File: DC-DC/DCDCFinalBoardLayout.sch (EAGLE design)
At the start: 38 parts, among them K1 ALZ12B12W, Q1 BUZ10, Q2 BUZ10

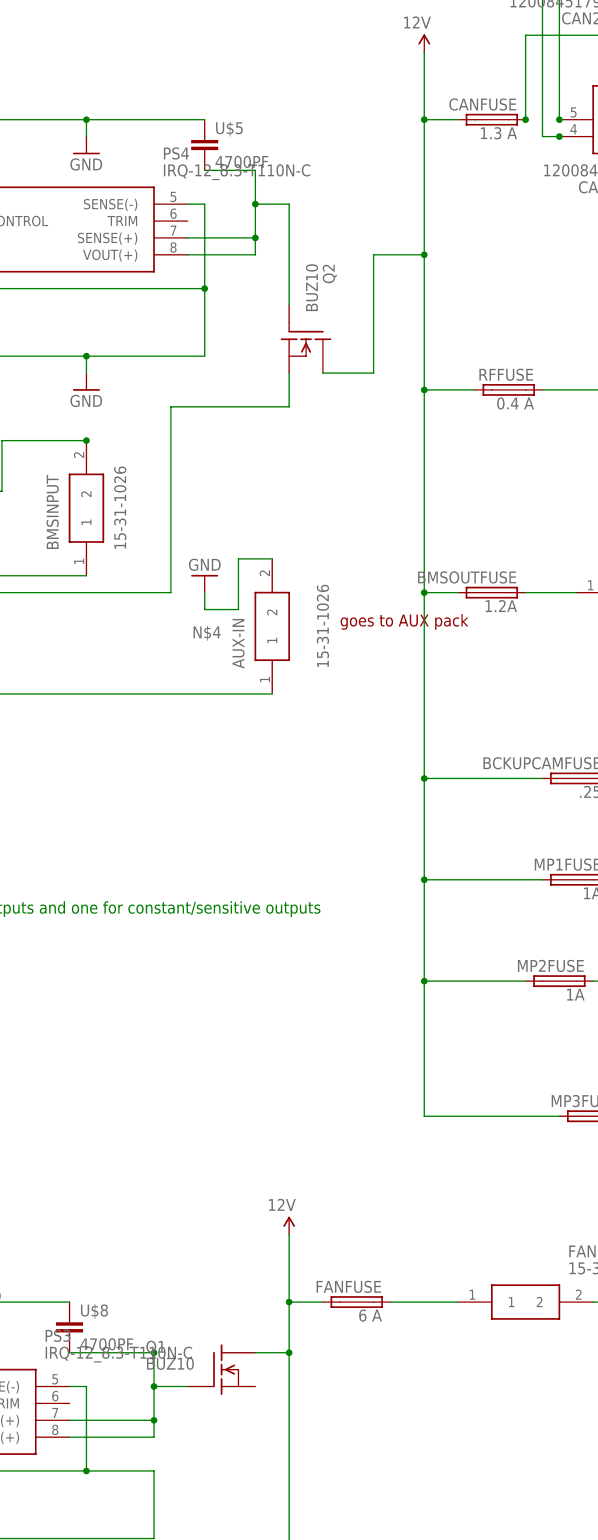
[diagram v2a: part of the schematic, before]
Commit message: updated DCDC diode
replaced insufficient SMD diode (in terms of current cap) with three TO220 diodes, with parallel dual configurations
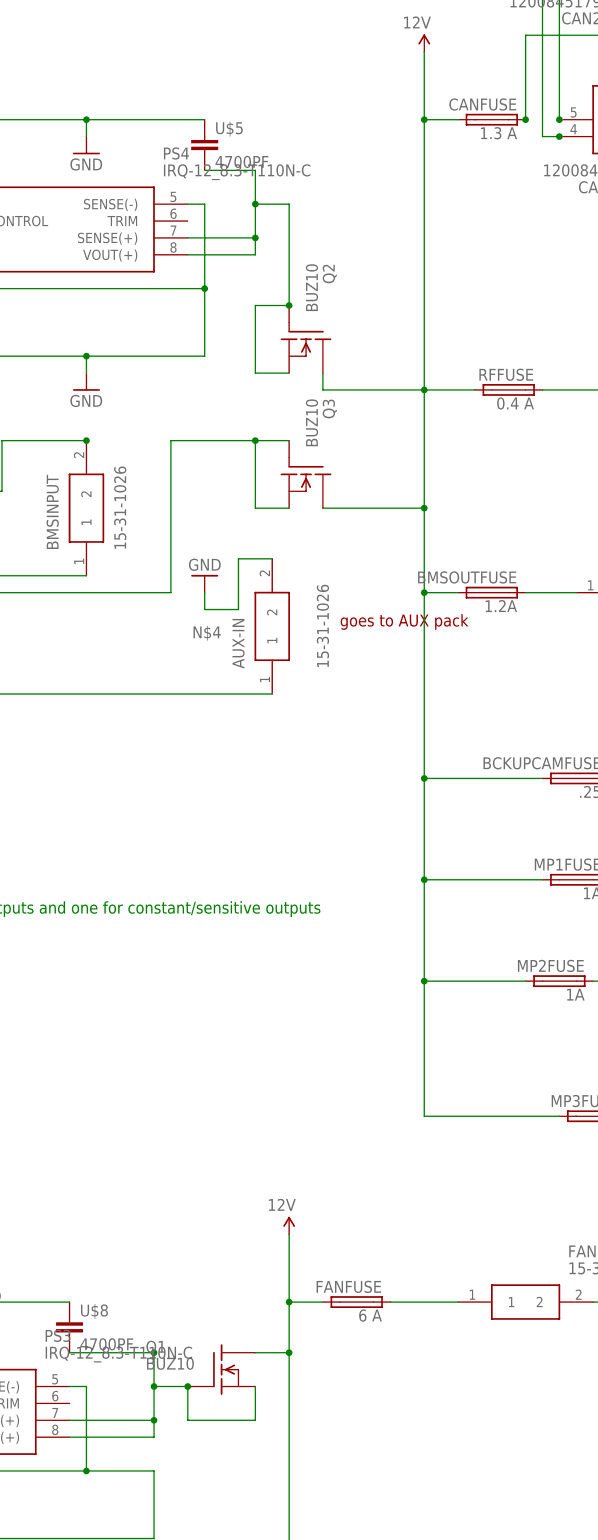
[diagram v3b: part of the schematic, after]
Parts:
- added Q3: BUZ10, transistor-fet:BUZ10
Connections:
- net 12V: now also Q3.D
- net N$13: now also Q1.S
- net N$15: now also Q2.S
- net N$4: now also Q3.G, Q3.S; no longer Q2.S
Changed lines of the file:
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@@
 <?xml version="1.0" encoding="utf-8"?>
 <!DOCTYPE eagle SYSTEM "eagle.dtd">
-<eagle version="9.5.1">
+<eagle version="9.1.1">
 <drawing>
 <settings>
@@
 <part name="Q2" library="transistor-fet" library_urn="urn:adsk.eagle:library:396" deviceset="BUZ10" device="" package3d_urn="urn:adsk.eagle:package:28520/1"/>
 <part name="Q1" library="transistor-fet" library_urn="urn:adsk.eagle:library:396" deviceset="BUZ10" device="" package3d_urn="urn:adsk.eagle:package:28520/1"/>
+<part name="Q3" library="transistor-fet" library_urn="urn:adsk.eagle:library:396" deviceset="BUZ10" device="" package3d_urn="urn:adsk.eagle:package:28520/1"/>
 </parts>
 <sheets>
@@
 <attribute name="VALUE" x="-204.47" y="-50.8" size="1.778" layer="96"/>
 <attribute name="NAME" x="-204.47" y="-48.26" size="1.778" layer="95"/>
+</instance>
+<instance part="Q3" gate="G$1" x="-180.34" y="83.82" smashed="yes" rot="R270">
+<attribute name="VALUE" x="-180.34" y="95.25" size="1.778" layer="96" rot="R270"/>
+<attribute name="NAME" x="-177.8" y="95.25" size="1.778" layer="95" rot="R270"/>
 </instance>
 </instances>
@@
 <wire x1="-162.56" y1="137.16" x2="-162.56" y2="147.32" width="0.1524" layer="91"/>
 <junction x="-162.56" y="137.16"/>
-<wire x1="-162.56" y1="137.16" x2="-162.56" y2="116.84" width="0.1524" layer="91"/>
-<wire x1="-162.56" y1="116.84" x2="-162.56" y2="96.52" width="0.1524" layer="91"/>
+<wire x1="-162.56" y1="137.16" x2="-162.56" y2="96.52" width="0.1524" layer="91"/>
 <pinref part="RFFUSE" gate="F1" pin="2"/>
 <wire x1="-162.56" y1="96.52" x2="-154.94" y2="96.52" width="0.1524" layer="91"/>
 <junction x="-162.56" y="96.52"/>
-<wire x1="-170.18" y1="116.84" x2="-162.56" y2="116.84" width="0.1524" layer="91"/>
-<junction x="-162.56" y="116.84"/>
 <pinref part="MP3FUSE" gate="F1" pin="2"/>
 <wire x1="-162.56" y1="-12.7" x2="-142.24" y2="-12.7" width="0.1524" layer="91"/>
@@
 <wire x1="-162.56" y1="38.1" x2="-162.56" y2="66.04" width="0.1524" layer="91"/>
 <pinref part="BMSOUTFUSE" gate="F1" pin="2"/>
-<wire x1="-162.56" y1="66.04" x2="-162.56" y2="96.52" width="0.1524" layer="91"/>
+<wire x1="-162.56" y1="66.04" x2="-162.56" y2="78.74" width="0.1524" layer="91"/>
+<wire x1="-162.56" y1="78.74" x2="-162.56" y2="96.52" width="0.1524" layer="91"/>
 <wire x1="-162.56" y1="66.04" x2="-157.48" y2="66.04" width="0.1524" layer="91"/>
 <junction x="-162.56" y="66.04"/>
 <junction x="-162.56" y="38.1"/>
 <pinref part="Q2" gate="G$1" pin="D"/>
-<wire x1="-177.8" y1="99.06" x2="-170.18" y2="99.06" width="0.1524" layer="91"/>
-<wire x1="-170.18" y1="99.06" x2="-170.18" y2="116.84" width="0.1524" layer="91"/>
+<wire x1="-177.8" y1="99.06" x2="-177.8" y2="96.52" width="0.1524" layer="91"/>
+<wire x1="-177.8" y1="96.52" x2="-162.56" y2="96.52" width="0.1524" layer="91"/>
+<pinref part="Q3" gate="G$1" pin="D"/>
+<wire x1="-177.8" y1="78.74" x2="-162.56" y2="78.74" width="0.1524" layer="91"/>
+<junction x="-162.56" y="78.74"/>
 </segment>
 <segment>
@@
 <label x="-193.04" y="60.96" size="1.778" layer="95" rot="R180"/>
 <pinref part="K1" gate="G$1" pin="NC_2"/>
-<wire x1="-200.66" y1="93.98" x2="-200.66" y2="66.04" width="0.1524" layer="91"/>
 <wire x1="-200.66" y1="66.04" x2="-241.3" y2="66.04" width="0.1524" layer="91"/>
-<wire x1="-200.66" y1="93.98" x2="-182.88" y2="93.98" width="0.1524" layer="91"/>
-<pinref part="Q2" gate="G$1" pin="S"/>
-<wire x1="-182.88" y1="93.98" x2="-182.88" y2="99.06" width="0.1524" layer="91"/>
+<pinref part="Q3" gate="G$1" pin="G"/>
+<wire x1="-200.66" y1="66.04" x2="-200.66" y2="88.9" width="0.1524" layer="91"/>
+<wire x1="-200.66" y1="88.9" x2="-187.96" y2="88.9" width="0.1524" layer="91"/>
+<wire x1="-187.96" y1="88.9" x2="-182.88" y2="88.9" width="0.1524" layer="91"/>
+<wire x1="-187.96" y1="88.9" x2="-187.96" y2="78.74" width="0.1524" layer="91"/>
+<junction x="-187.96" y="88.9"/>
+<pinref part="Q3" gate="G$1" pin="S"/>
+<wire x1="-187.96" y1="78.74" x2="-182.88" y2="78.74" width="0.1524" layer="91"/>
 </segment>
 </net>
@@
 <wire x1="-182.88" y1="124.46" x2="-182.88" y2="109.22" width="0.1524" layer="91"/>
 <junction x="-187.96" y="124.46"/>
+<pinref part="Q2" gate="G$1" pin="S"/>
+<wire x1="-182.88" y1="99.06" x2="-187.96" y2="99.06" width="0.1524" layer="91"/>
+<wire x1="-187.96" y1="99.06" x2="-187.96" y2="109.22" width="0.1524" layer="91"/>
+<wire x1="-187.96" y1="109.22" x2="-182.88" y2="109.22" width="0.1524" layer="91"/>
+<junction x="-182.88" y="109.22"/>
 </segment>
 </net>
@@
 <junction x="-203.2" y="-53.34"/>
 <pinref part="Q1" gate="G$1" pin="G"/>
-</segment>
-</net>
+<pinref part="Q1" gate="G$1" pin="S"/>
+<wire x1="-187.96" y1="-53.34" x2="-187.96" y2="-58.42" width="0.1524" layer="91"/>
+<wire x1="-187.96" y1="-58.42" x2="-198.12" y2="-58.42" width="0.1524" layer="91"/>
+<wire x1="-198.12" y1="-58.42" x2="-198.12" y2="-53.34" width="0.1524" layer="91"/>
+<junction x="-198.12" y="-53.34"/>
+</segment>
+</net>
